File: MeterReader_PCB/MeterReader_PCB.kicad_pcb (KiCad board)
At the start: 2 copper layers, 0 parts

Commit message: move active components onto sensor PCB, finish layout of sensor PCB
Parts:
- added BT1: 3.7V LiIon, Battery:BatteryHolder_Keystone_1042_1x18650, F.Cu at (113.5, 103.0)
- added BT2: 3.7V LiIon, Battery:BatteryHolder_Keystone_1042_1x18650, F.Cu at (113.5, 124.1)
- added BT3: 3.7V LiIon, Battery:BatteryHolder_Keystone_1042_1x18650, B.Cu at (113.5, 124.1)
- added BT4: 3.7V LiIon, Battery:BatteryHolder_Keystone_1042_1x18650, B.Cu at (113.5, 103.0)
- added C1: 12p, Capacitor_SMD:C_0603_1608Metric, F.Cu at (101.1, 85.8)
- added C2: 12p, Capacitor_SMD:C_0603_1608Metric, F.Cu at (107.0, 86.0)
- added C3: 1u, Capacitor_SMD:C_0603_1608Metric, F.Cu at (157.0, 130.9)
- added C4: 100n, Capacitor_SMD:C_0603_1608Metric, F.Cu at (162.2, 103.1)
- added D1: SS34, Diode_SMD:D_SMA, F.Cu at (154.2, 131.2)
- added D10: LED, LED_SMD:LED_0603_1608Metric, F.Cu at (117.5, 82.7)
- added D2: SS34, Diode_SMD:D_SMA, F.Cu at (154.6, 95.7)
- added D3: SS34, Diode_SMD:D_SMA, F.Cu at (160.6, 122.3)
- added D4: SS34, Diode_SMD:D_SMA, F.Cu at (160.6, 126.2)
- added D5: SS34, Diode_SMD:D_SMA, B.Cu at (101.2, 147.9)
- added D6: SS34, Diode_SMD:D_SMA, B.Cu at (71.0, 141.9)
- added D7: SS34, Diode_SMD:D_SMA, B.Cu at (93.1, 147.9)
- added D8: SS34, Diode_SMD:D_SMA, B.Cu at (71.0, 146.5)
- added J1: USB_C_Receptacle_USB2.0, Connector_USB:USB_C_Receptacle_HRO_TYPE-C-31-M-12, F.Cu at (126.2, 77.7)
- added J2: SWD_TagConnect, LeoDJ-kicad:Paw-Connect_TC2030-IDC-NL_2x03_P1.27mm_Vertical, F.Cu at (117.0, 86.8)
- added J3: SWD, Connector_PinHeader_2.54mm:PinHeader_1x04_P2.54mm_Vertical, F.Cu at (116.4, 74.0)
- added J6: Conn_01x02, Connector_JST:JST_PH_S2B-PH-K_1x02_P2.00mm_Horizontal, F.Cu at (123.6, 69.4)
- added J7: Conn_01x02, Connector_JST:JST_PH_S2B-PH-K_1x02_P2.00mm_Horizontal, F.Cu at (161.6, 98.2)
- added J8: USB_C_Receptacle_USB2.0, Connector_USB:USB_C_Receptacle_HRO_TYPE-C-31-M-12, F.Cu at (159.9, 114.8)
- added LOGO1: Logo_Open_Hardware_Small, Symbol:OSHW-Symbol_6.7x6mm_SilkScreen, B.Cu at (105.1, 84.3)
- added Q1: Q_NMOS_GSD, Package_TO_SOT_SMD:SOT-23, B.Cu at (118.8, 81.1)
- added Q2: AO3401A, Package_TO_SOT_SMD:SOT-23, F.Cu at (119.9, 69.7)
- added Q3: FS8205A, Package_SO:TSSOP-8_4.4x3mm_P0.65mm, F.Cu at (158.9, 104.8)
- added R1: 5k1, Resistor_SMD:R_0603_1608Metric, F.Cu at (120.3, 79.7)
- added R10: 1k, Capacitor_SMD:C_0603_1608Metric, F.Cu at (162.2, 108.7)
- added R11: 5k1, Resistor_SMD:R_0603_1608Metric, F.Cu at (153.5, 117.1)
- added R12: 5k1, Resistor_SMD:R_0603_1608Metric, F.Cu at (153.5, 112.0)
- added R2: 5k1, Resistor_SMD:R_0603_1608Metric, F.Cu at (120.3, 75.2)
- added R3: 5k1, Resistor_SMD:R_0603_1608Metric, B.Cu at (118.8, 78.3)
- added R4: 33, Resistor_SMD:R_0603_1608Metric, B.Cu at (112.3, 82.9)
- added R5: 100k, Resistor_SMD:R_0603_1608Metric, B.Cu at (112.3, 78.5)
- added R6: 100k, Resistor_SMD:R_0603_1608Metric, F.Cu at (119.9, 66.9)
- added R7: 5k1, Resistor_SMD:R_0603_1608Metric, F.Cu at (118.5, 79.7)
- added R8: 2k2, Resistor_SMD:R_0603_1608Metric, F.Cu at (163.0, 131.0)
- added R9: 100, Capacitor_SMD:C_0603_1608Metric, F.Cu at (162.2, 101.6)
- added REF**: Tag-Connect_TC2030-IDC-NL_2x03_P1.27mm_Vertical, Connector:Tag-Connect_TC2030-IDC-NL_2x03_P1.27mm_Vertical, F.Cu at (94.3, 75.8)
- added SW2: SW_Push, Button_Switch_SMD:SW_SPST_TL3342, F.Cu at (125.0, 86.2)
- added TP1: TestPoint, TestPoint:TestPoint_Pad_1.5x1.5mm, F.Cu at (116.4, 79.1)
- added TP2: TestPoint, TestPoint:TestPoint_Pad_1.5x1.5mm, F.Cu at (116.4, 76.6)
- added U1: QRE1113GR, OptoDevice:OnSemi_CASE100CY, B.Cu at (115.0, 80.0)
- added U2: E73-2G4M08S1C, E73-2G4M08S1C:E73-2G4M08S1C, F.Cu at (107.6, 74.4)
- added U3: LTC4054ES5-4.2, Package_TO_SOT_SMD:TSOT-23-5, F.Cu at (159.9, 131.3)
- added U4: DW01A, Package_TO_SOT_SMD:SOT-23-6, F.Cu at (162.4, 105.9)
- added Y1: 32.768kHz, Crystal:Crystal_SMD_3215-2Pin_3.2x1.5mm, F.Cu at (104.1, 85.7)
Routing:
- net RESET: track 0.00 -> 64.6 mm, vias 0 -> 1
- net /MCU/Button_1: track 0.00 -> 50.5 mm, vias 0 -> 2
- net +BATT: track 0.00 -> 49.8 mm
- net SWDIO: track 0.00 -> 29.3 mm, vias 0 -> 1
- net +BATT_RAW: track 0.00 -> 28.3 mm
- net SWCLK: track 0.00 -> 22.4 mm, vias 0 -> 1
- net /MCU/UART_TX: track 0.00 -> 22.4 mm, vias 0 -> 2
- net +1V8: track 0.00 -> 21.5 mm, vias 0 -> 2
- net /MCU/Sensor_LED: track 0.00 -> 21.2 mm, vias 0 -> 1
- net /MCU/UART_RX: track 0.00 -> 17.4 mm
- net /MCU/LED_0: track 0.00 -> 17.1 mm, vias 0 -> 2
- net /MCU/Sensor_Signal: track 0.00 -> 13.2 mm, vias 0 -> 1
- net /MCU/USB_DP: track 0.00 -> 12.4 mm
- net /MCU/USB_DM: track 0.00 -> 11.7 mm
- net GND: track 0.00 -> 11.3 mm, vias 0 -> 3
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- added copper zone on B.Cu, net GND
- added copper zone on F.Cu, net GND
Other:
- board outline added: 94.5 x 69.8 mm

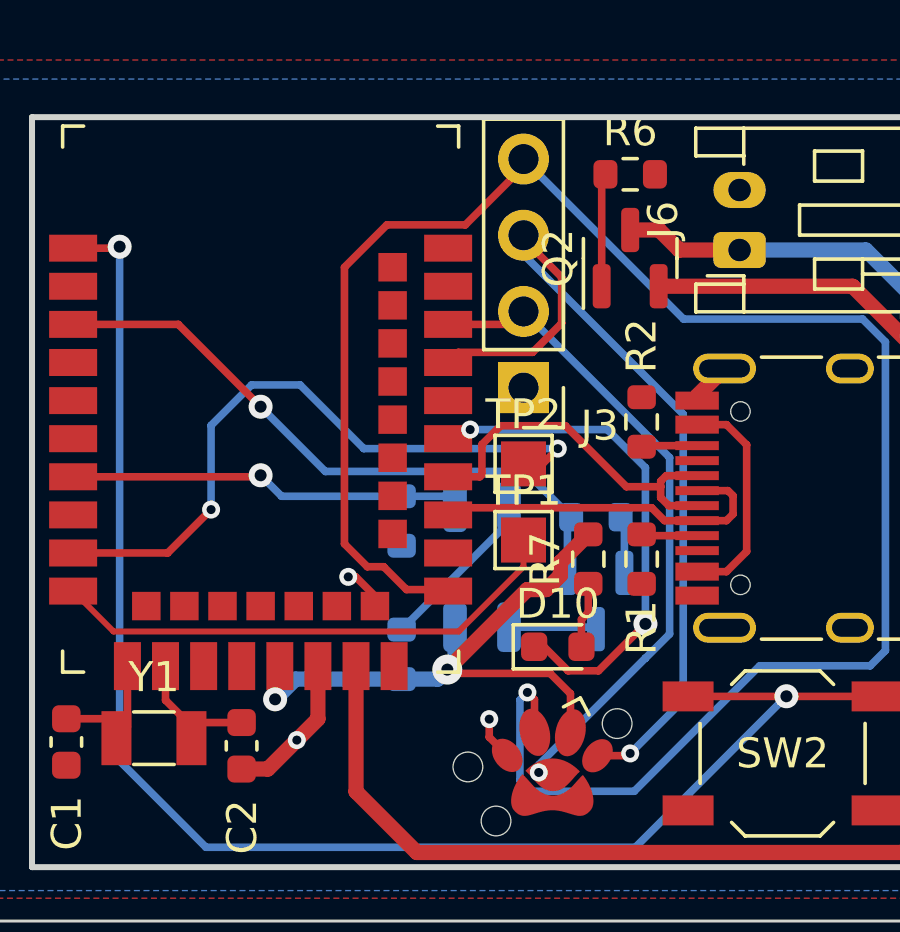
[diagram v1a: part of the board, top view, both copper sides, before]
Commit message: add VBUS diode and trace to MCU
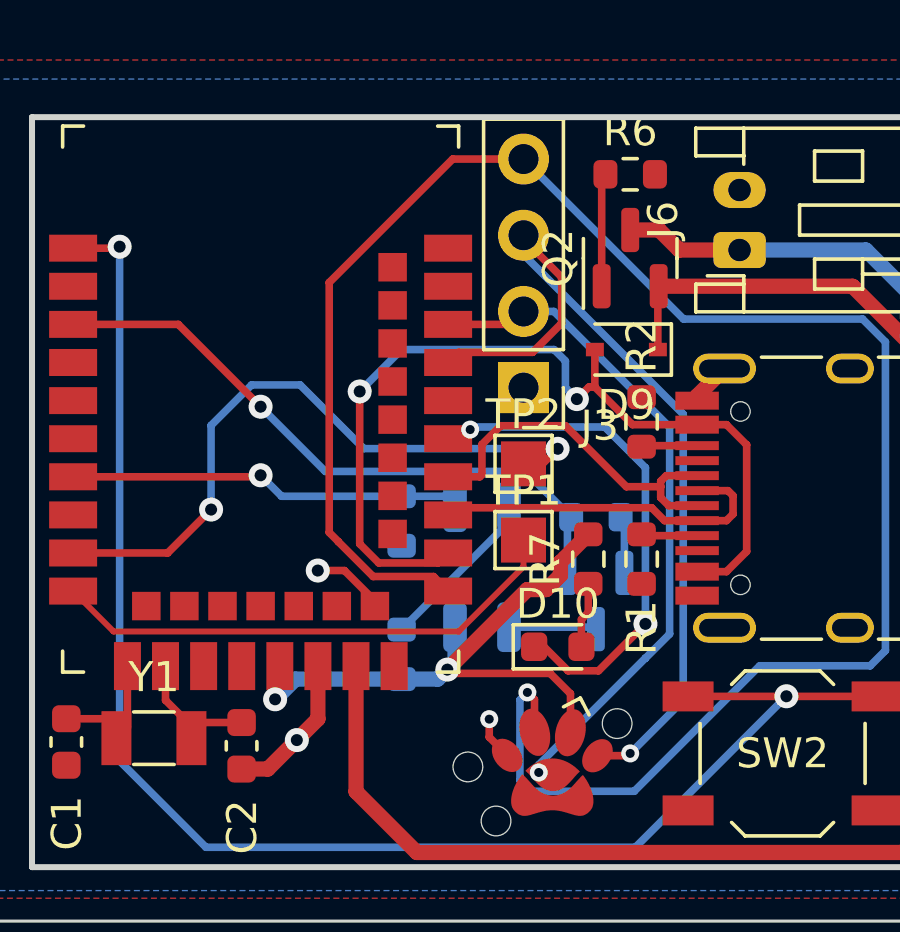
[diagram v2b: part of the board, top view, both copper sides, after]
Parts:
- added D9: D_Schottky, Diode_SMD:D_SOD-323, F.Cu at (119.8, 72.7)
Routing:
- net VBUS: track 7.42 -> 30.8 mm, vias 0 -> 2
- net +BATT: track 49.8 -> 51.9 mm
- net GND: track 11.3 -> 12.3 mm
- net SWCLK: track 22.4 -> 23.0 mm

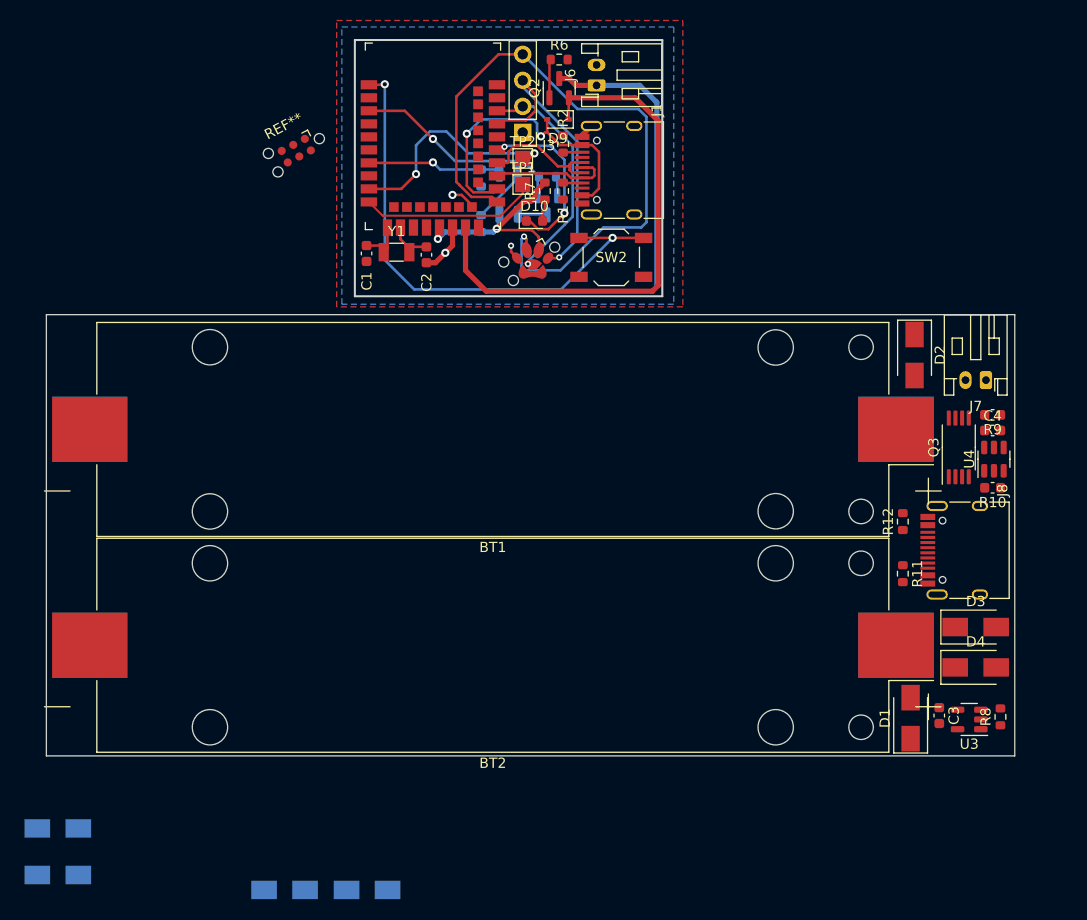
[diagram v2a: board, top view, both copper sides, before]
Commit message: finish layout of battery pack PCB
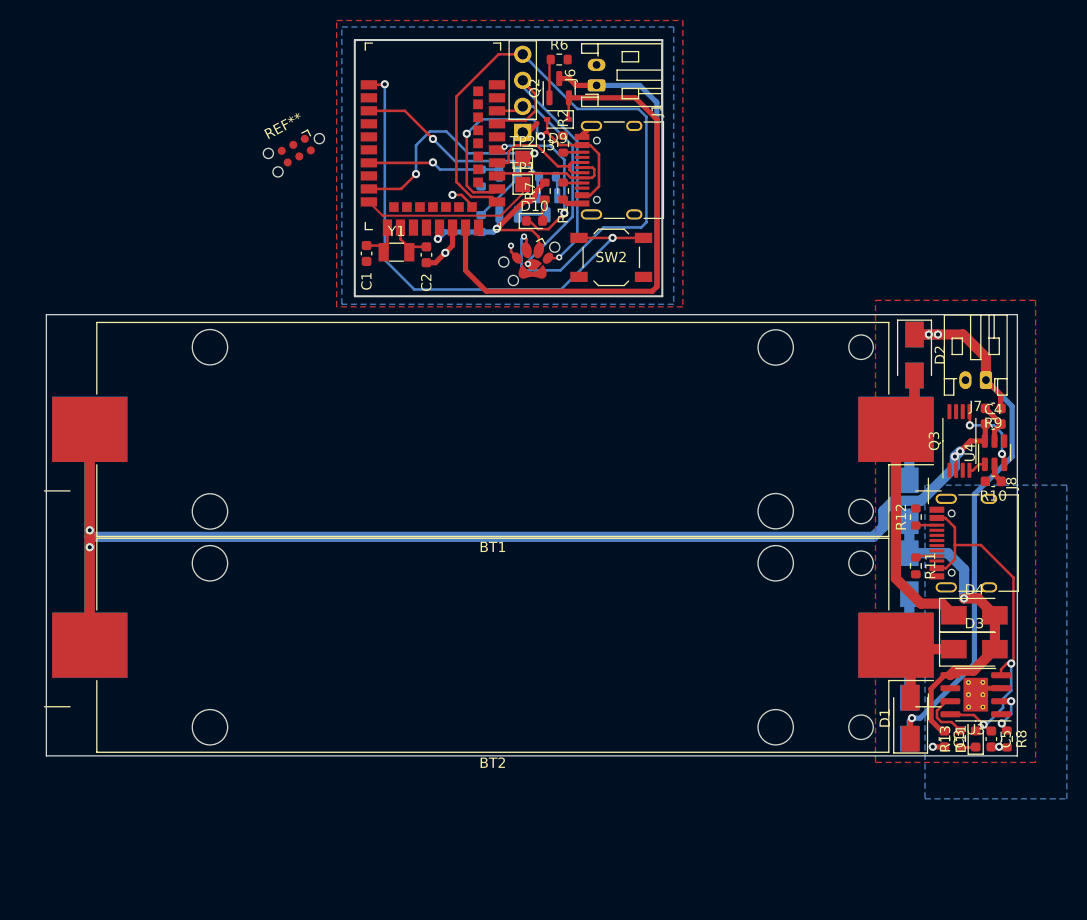
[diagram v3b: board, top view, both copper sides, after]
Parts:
- added C5: 1u, Capacitor_SMD:C_0603_1608Metric, F.Cu at (162.1, 133.2)
- added D11: LED_Red, LED_SMD:LED_0603_1608Metric, F.Cu at (160.6, 133.2)
- added R13: 1k, Resistor_SMD:R_0603_1608Metric, F.Cu at (159.1, 133.2)
- R8: value 2k2 -> 1k1
- U3: value LTC4054ES5-4.2 -> TP4056; footprint Package_TO_SOT_SMD:TSOT-23-5 -> Package_SO:SOIC-8-1EP_3.9x4.9mm_P1.27mm_EP2.41x3.3mm_ThermalVias
- moved D8 97.8 mm to (154.6, 95.7), turned to -90 degrees
- moved D6 83.8 mm to (154.1, 131.2), turned to 90 degrees
- moved D7 71.8 mm to (154.1, 110.0), turned to -90 degrees
- moved D5 61.3 mm to (154.1, 117.1), turned to 90 degrees
- moved D4 5.08 mm to (160.5, 121.1)
- moved U3 2.50 mm to (160.6, 128.9)
- moved C3 2.34 mm to (157.5, 133.2)
- moved R8 2.25 mm to (163.6, 133.2), turned to -90 degrees
- moved D3 2.16 mm to (160.5, 124.4)
- moved R11 1.48 mm to (154.7, 116.3)
- moved R12 1.35 mm to (154.7, 111.5)
- moved J8 1.13 mm to (160.8, 114.1)
- moved Q3 0.63 mm to (159.0, 104.1)
- moved R10 0.63 mm to (162.3, 108.1)
- moved U4 0.63 mm to (162.4, 105.3)
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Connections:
- C3 pad 1: VBUS -> +BATT_CHG
- U3 pad 2: GND -> Net-(R8-Pad1)
- U3 pad 3: +BATT_CHG -> GND
- U3 pad 5: Net-(R8-Pad1) -> +BATT_CHG
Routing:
- net -BATT_RAW: track 0.00 -> 137.9 mm, vias 0 -> 4
- net +BATT_RAW: track 28.3 -> 86.8 mm, vias 0 -> 3
- net VBUS: track 30.8 -> 68.2 mm, vias 2 -> 4
- net +BATT_CHG: track 0.00 -> 31.6 mm, vias 0 -> 1
- net Net-(BT1-Pad1): track 0.00 -> 27.7 mm
- net Net-(BT2-Pad1): track 0.00 -> 11.5 mm
- net Net-(BT4-Pad1): track 0.00 -> 11.5 mm
- net Net-(BT3-Pad1): track 0.00 -> 11.2 mm
- net GND: track 12.3 -> 20.7 mm, vias 3 -> 5
- net Net-(Q3-Pad5): track 0.00 -> 7.93 mm, vias 0 -> 2
- net Net-(U3-Pad7): track 0.00 -> 5.15 mm
- net Net-(R8-Pad1): track 0.00 -> 4.44 mm, vias 0 -> 2
- net Net-(C4-Pad2): track 0.00 -> 4.11 mm
- net Net-(J8-PadA5): track 0.00 -> 2.11 mm
- net Net-(J8-PadB5): track 0.00 -> 2.07 mm
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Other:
- board size 94.5 x 69.8 mm -> 94.7 x 69.8 mm

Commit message: finish track layout of battery module && merge both modules
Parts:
- added mouse-bite-2mm-slot: VAL**, Panelization:mouse-bite-2mm-slot, F.Cu at (122.5, 91.0)
- added mouse-bite-2mm-slot: VAL**, Panelization:mouse-bite-2mm-slot, F.Cu at (107.5, 91.0)
- moved C5 3.17 mm to (158.9, 133.4)
- moved D11 3.17 mm to (157.4, 133.4)
- moved R13 3.17 mm to (155.9, 133.4)
- moved R8 3.17 mm to (160.5, 133.4)
- moved C3 3.17 mm to (154.4, 133.4)
- moved C4 2.29 mm to (160.0, 102.7)
- moved D1 2.29 mm to (152.0, 131.4)
- moved D2 2.29 mm to (152.3, 95.9)
- moved D4 2.29 mm to (158.2, 121.3)
- moved D5 2.29 mm to (151.8, 117.3)
- moved D6 2.29 mm to (151.8, 131.4)
- moved D7 2.29 mm to (151.8, 110.2)
- moved D8 2.29 mm to (152.3, 95.9)
- moved J7 2.29 mm to (159.3, 98.4)
- moved J8 2.29 mm to (158.6, 114.3)
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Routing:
- net VBUS: track 68.2 -> 151.8 mm, vias 4 -> 6
- net GND: track 20.7 -> 69.0 mm, vias 5 -> 7
- net +BATT_RAW: track 86.8 -> 122.2 mm
- net +BATT: track 51.8 -> 47.9 mm
- net RESET: track 64.9 -> 62.6 mm
- net /MCU/Button_1: track 50.5 -> 48.2 mm
- net +1V8: track 21.5 -> 22.7 mm
- net Net-(U3-Pad7): track 5.15 -> 4.26 mm
- net +BATT_CHG: track 31.6 -> 31.1 mm
- added copper zone on B.Cu, net +BATT_RAW
- added copper zone on B.Cu, net VBUS
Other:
- board size 94.7 x 69.8 mm -> 94.8 x 70 mm
